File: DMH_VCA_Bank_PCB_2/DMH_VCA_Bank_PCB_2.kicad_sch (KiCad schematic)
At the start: 0 parts

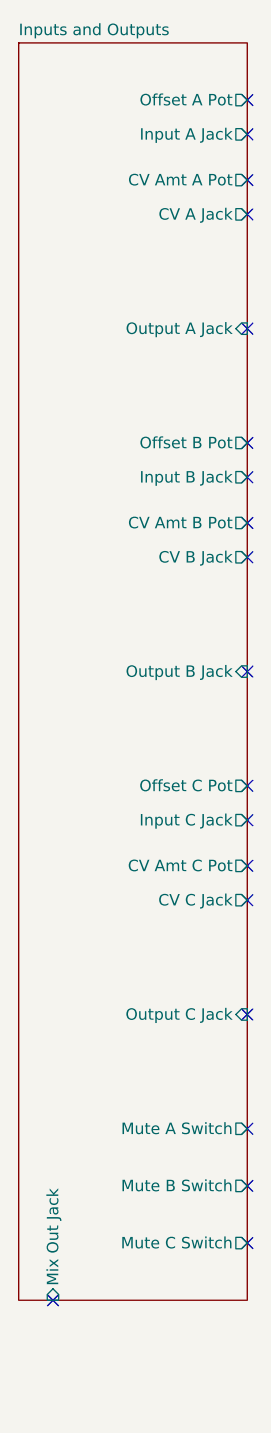
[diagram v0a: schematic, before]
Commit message: Finished schematic of PCB 2
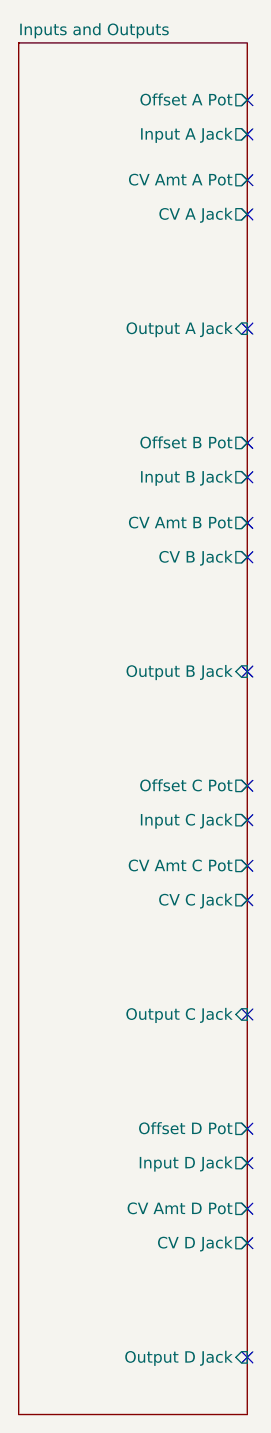
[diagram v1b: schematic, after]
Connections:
- no-connect marks 19 -> 20
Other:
- sheet Inputs and Outputs ports: added CV Amt D Pot, CV D Jack, Input D Jack, Offset D Pot, Output D Jack; removed Mix Out Jack, Mute A Switch, Mute B Switch, Mute C Switch
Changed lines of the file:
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@@
 	)
 	(no_connect
-		(at 50.8 152.4)
+		(at 50.8 149.86)
 	)
 	(no_connect
@@
 	)
 	(no_connect
-		(at 29.21 165.1)
-	)
-	(no_connect
 		(at 50.8 146.05)
 	)
@@
 	)
 	(no_connect
+		(at 50.8 154.94)
+	)
+	(no_connect
 		(at 50.8 107.95)
 	)
 	(no_connect
 		(at 50.8 40.64)
+	)
+	(no_connect
+		(at 50.8 171.45)
 	)
 	(no_connect
@@
 	(sheet
 		(at 25.4 25.4)
-		(size 25.4 139.7)
+		(size 25.4 152.4)
 		(exclude_from_sim no)
 		(in_bom yes)
@@
 		)
 		(property "Sheetfile" "Inputs_and_Outputs.kicad_sch"
-			(at 25.4 165.6846 0)
+			(at 25.4 178.3846 0)
 			(effects
 				(font
@@
 			)
 		)
-		(pin "Mute B Switch" output
-			(at 50.8 152.4 0)
-			(effects
-				(font
-					(size 1.27 1.27)
-				)
-				(justify right)
-			)
-		)
 		(pin "Offset B Pot" output
 			(at 50.8 69.85 0)
@@
 			)
 		)
-		(pin "Mute C Switch" output
-			(at 50.8 158.75 0)
-			(effects
-				(font
-					(size 1.27 1.27)
-				)
-				(justify right)
-			)
-		)
 		(pin "Input C Jack" output
 			(at 50.8 111.76 0)
@@
 			)
 		)
-		(pin "Mute A Switch" output
-			(at 50.8 146.05 0)
-			(effects
-				(font
-					(size 1.27 1.27)
-				)
-				(justify right)
-			)
-		)
 		(pin "Offset A Pot" output
 			(at 50.8 31.75 0)
@@
 			)
 		)
-		(pin "Mix Out Jack" input
-			(at 29.21 165.1 270)
-			(effects
-				(font
-					(size 1.27 1.27)
-				)
-				(justify left)
-			)
-		)
 		(pin "CV Amt A Pot" output
 			(at 50.8 40.64 0)
@@
 			(effects
 				(font
+					(size 1.27 1.27)
+				)
+				(justify right)
+			)
+		)
+		(pin "CV Amt D Pot" output
+			(at 50.8 154.94 0)
+			(effects
+				(font
+					(size 1.27 1.27)
+				)
+				(justify right)
+			)
+		)
+		(pin "CV D Jack" output
+			(at 50.8 158.75 0)
+			(effects
+				(font
+					(size 1.27 1.27)
+				)
+				(justify right)
+			)
+		)
+		(pin "Input D Jack" output
+			(at 50.8 149.86 0)
+			(effects
+				(font
+					(size 1.27 1.27)
+				)
+				(justify right)
+			)
+		)
+		(pin "Offset D Pot" output
+			(at 50.8 146.05 0)
+			(effects
+				(font
+					(size 1.27 1.27)
+				)
+				(justify right)
+			)
+		)
+		(pin "Output D Jack" input
+			(at 50.8 171.45 0)
+			(effects
+				(font
